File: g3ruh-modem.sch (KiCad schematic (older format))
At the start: 59 parts, among them Q1 LM7805_TO220, U1 4029, U10 LM339, U11 74HC14, U12 74HC164, U16 TL084, U2 27C128, U3 4029, U4 74HC164, U5 74HC74, U6 74HC86, U7 74HC164, U8 74HC161, U9 ZN429E-8

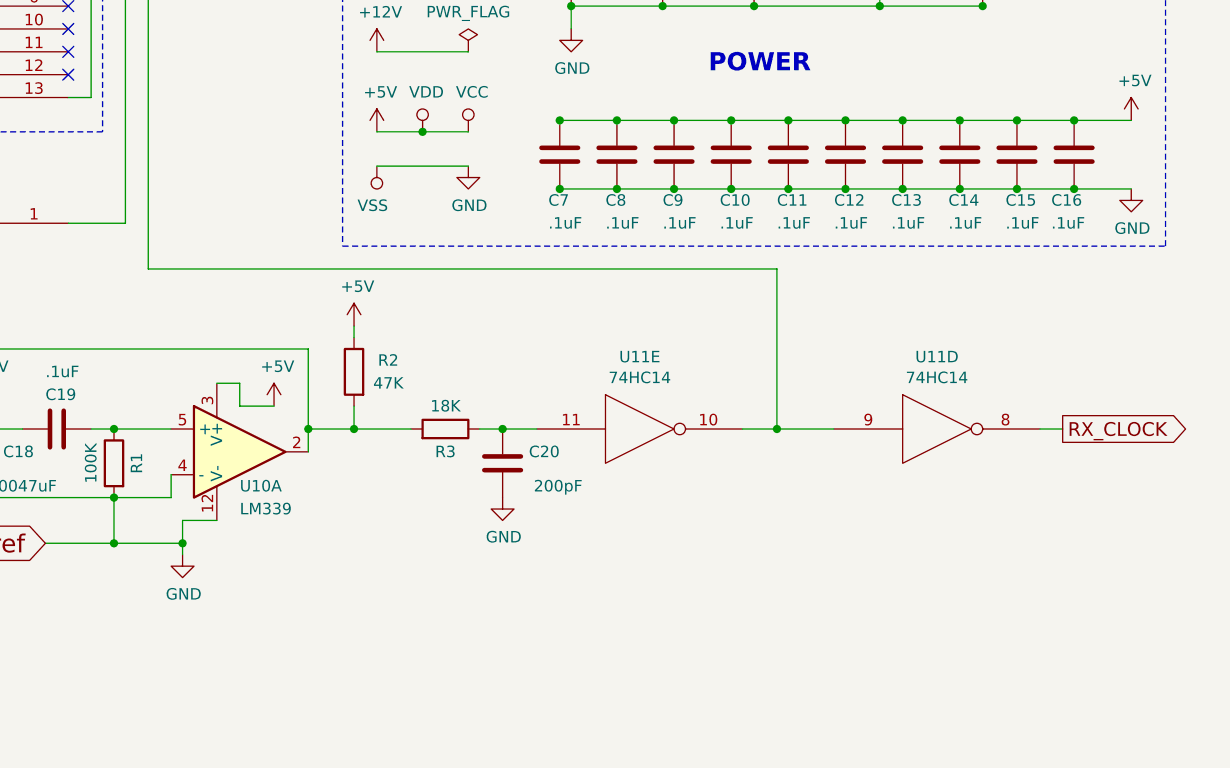
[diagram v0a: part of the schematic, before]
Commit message: Parts in roughly the right places and footprints verified.
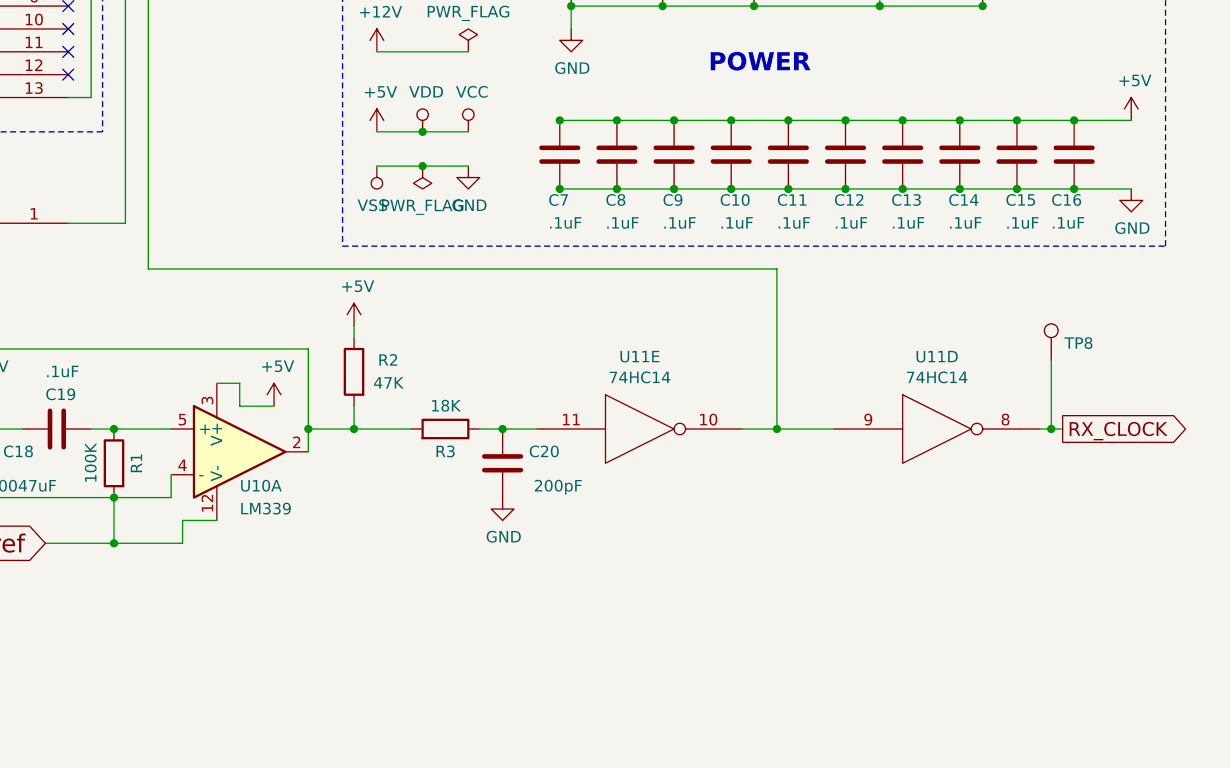
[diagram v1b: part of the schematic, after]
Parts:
- added TP8: TEST_1P, Connectors:PINTST, symbol TEST_1P
- C18, C19, C20, C21, C22: footprint Capacitors_THT:C_Axial_L3.8mm_D2.6mm_P10.00mm_Horizontal -> Capacitors_THT:C_Disc_D3.0mm_W2.0mm_P2.50mm
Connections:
- net GND: no longer C18.2, C26.2, C28.2, R1.2, R16.2, U10.12 (V-), U10.4 (-), U10.6 (-)
- net RX_CLOCK: now also TP8.1
- new net Vref: C18.2, C26.2, C28.2, R1.2, R16.2, U10.12 (V-), U10.4 (-), U10.6 (-)
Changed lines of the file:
@@
 F 0 "C22" H 8815 2646 50  0000 L CNN
 F 1 ".1uF" H 8815 2555 50  0000 L CNN
-F 2 "Capacitors_THT:C_Axial_L3.8mm_D2.6mm_P10.00mm_Horizontal" H 8738 2450 50  0001 C CNN
+F 2 "Capacitors_THT:C_Disc_D3.0mm_W2.0mm_P2.50mm" H 8738 2450 50  0001 C CNN
 F 3 "" H 8700 2600 50  0001 C CNN
 F 4 "20% monolithic" V 8700 2600 60  0001 C CNN "Type"
@@
 F 0 "C21" H 8415 2646 50  0000 L CNN
 F 1 ".1uF" H 8415 2555 50  0000 L CNN
-F 2 "Capacitors_THT:C_Axial_L3.8mm_D2.6mm_P10.00mm_Horizontal" H 8338 2450 50  0001 C CNN
+F 2 "Capacitors_THT:C_Disc_D3.0mm_W2.0mm_P2.50mm" H 8338 2450 50  0001 C CNN
 F 3 "" H 8300 2600 50  0001 C CNN
 F 4 "20% monolithic" V 8300 2600 60  0001 C CNN "Type"
@@
 F 0 "C18" H 5650 6150 50  0000 L CNN
 F 1 ".0047uF" H 5550 6000 50  0000 L CNN
-F 2 "Capacitors_THT:C_Axial_L3.8mm_D2.6mm_P10.00mm_Horizontal" H 5938 5950 50  0001 C CNN
+F 2 "Capacitors_THT:C_Disc_D3.0mm_W2.0mm_P2.50mm" H 5938 5950 50  0001 C CNN
 F 3 "" H 5900 6100 50  0001 C CNN
 F 4 "20% monolithic" V 5900 6100 60  0001 C CNN "Type"
@@
 F 0 "C19" V 6100 5900 50  0000 L CNN
 F 1 ".1uF" V 6000 5900 50  0000 L CNN
-F 2 "Capacitors_THT:C_Axial_L3.8mm_D2.6mm_P10.00mm_Horizontal" H 6288 5800 50  0001 C CNN
+F 2 "Capacitors_THT:C_Disc_D3.0mm_W2.0mm_P2.50mm" H 6288 5800 50  0001 C CNN
 F 3 "" H 6250 5950 50  0001 C CNN
 F 4 "20% monolithic" V 6250 5950 60  0001 C CNN "Type"
@@
 	1    0    0    -1
 $EndComp
-$Comp
-L GND #PWR025
-U 1 1 5972B70D
-P 6800 6500
-F 0 "#PWR025" H 6800 6250 50  0001 C CNN
-F 1 "GND" H 6805 6327 50  0000 C CNN
-F 2 "" H 6800 6500 50  0001 C CNN
-F 3 "" H 6800 6500 50  0001 C CNN
-	1    6800 6500
-	1    0    0    -1
-$EndComp
 Wire Wire Line
 	6950 6350 6800 6350
-Wire Wire Line
-	6800 6350 6800 6500
 Wire Wire Line
 	6400 5950 6750 5950
@@
 	7050 5850 7200 5850
 $Comp
-L +5V #PWR026
+L +5V #PWR025
 U 1 1 59730602
 P 7550 5500
-F 0 "#PWR026" H 7550 5350 50  0001 C CNN
+F 0 "#PWR025" H 7550 5350 50  0001 C CNN
 F 1 "+5V" H 7565 5673 50  0000 C CNN
 F 2 "" H 7550 5500 50  0001 C CNN
@@
 F 0 "C20" H 7950 6150 50  0000 L CNN
 F 1 "200pF" H 7850 6000 50  0000 L CNN
-F 2 "Capacitors_THT:C_Axial_L3.8mm_D2.6mm_P10.00mm_Horizontal" H 8238 5950 50  0001 C CNN
+F 2 "Capacitors_THT:C_Disc_D3.0mm_W2.0mm_P2.50mm" H 8238 5950 50  0001 C CNN
 F 3 "" H 8200 6100 50  0001 C CNN
 F 4 "20% monolithic" V 8200 6100 60  0001 C CNN "Type"
@@
 $EndComp
 $Comp
-L GND #PWR027
+L GND #PWR026
 U 1 1 597318B4
 P 8200 6250
-F 0 "#PWR027" H 8200 6000 50  0001 C CNN
+F 0 "#PWR026" H 8200 6000 50  0001 C CNN
 F 1 "GND" H 8205 6077 50  0000 C CNN
 F 2 "" H 8200 6250 50  0001 C CNN
@@
 	7950 3700 8100 3700
 $Comp
-L +5V #PWR028
+L +5V #PWR027
 U 1 1 596EEE17
 P 10300 3550
-F 0 "#PWR028" H 10300 3400 50  0001 C CNN
+F 0 "#PWR027" H 10300 3400 50  0001 C CNN
 F 1 "+5V" H 10315 3723 50  0000 C CNN
 F 2 "" H 10300 3550 50  0001 C CNN
@@
 	8450 4900 10950 4900
 $Comp
-L +5V #PWR029
+L +5V #PWR028
 U 1 1 596F0936
 P 10950 4600
-F 0 "#PWR029" H 10950 4450 50  0001 C CNN
+F 0 "#PWR028" H 10950 4450 50  0001 C CNN
 F 1 "+5V" H 10965 4773 50  0000 C CNN
 F 2 "" H 10950 4600 50  0001 C CNN
@@
 $EndComp
 $Comp
-L GND #PWR030
+L GND #PWR029
 U 1 1 596F10F5
 P 10950 4900
-F 0 "#PWR030" H 10950 4650 50  0001 C CNN
+F 0 "#PWR029" H 10950 4650 50  0001 C CNN
 F 1 "GND" H 10955 4727 50  0000 C CNN
 F 2 "" H 10950 4900 50  0001 C CNN
@@
 Connection ~ 8500 4100
 $Comp
-L GND #PWR031
+L GND #PWR030
 U 1 1 596F18F3
 P 8050 4800
-F 0 "#PWR031" H 8050 4550 50  0001 C CNN
+F 0 "#PWR030" H 8050 4550 50  0001 C CNN
 F 1 "GND" H 8055 4627 50  0000 C CNN
 F 2 "" H 8050 4800 50  0001 C CNN
@@
 Connection ~ 4050 3850
 $Comp
-L GND #PWR032
+L GND #PWR031
 U 1 1 597348D5
 P 1300 3700
-F 0 "#PWR032" H 1300 3450 50  0001 C CNN
+F 0 "#PWR031" H 1300 3450 50  0001 C CNN
 F 1 "GND" H 1305 3527 50  0000 C CNN
 F 2 "" H 1300 3700 50  0001 C CNN
@@
 $EndComp
 $Comp
-L GND #PWR033
+L GND #PWR032
 U 1 1 59734EC4
 P 1700 2950
-F 0 "#PWR033" H 1700 2700 50  0001 C CNN
+F 0 "#PWR032" H 1700 2700 50  0001 C CNN
 F 1 "GND" H 1705 2777 50  0000 C CNN
 F 2 "" H 1700 2950 50  0001 C CNN
@@
 $EndComp
 $Comp
-L GND #PWR034
+L GND #PWR033
 U 1 1 597366E0
 P 1300 4950
-F 0 "#PWR034" H 1300 4700 50  0001 C CNN
+F 0 "#PWR033" H 1300 4700 50  0001 C CNN
 F 1 "GND" H 1305 4777 50  0000 C CNN
 F 2 "" H 1300 4950 50  0001 C CNN
@@
 	1300 4850 1300 4950
 $Comp
-L GND #PWR035
+L GND #PWR034
 U 1 1 59737386
 P 3250 5050
-F 0 "#PWR035" H 3250 4800 50  0001 C CNN
+F 0 "#PWR034" H 3250 4800 50  0001 C CNN
 F 1 "GND" H 3255 4877 50  0000 C CNN
 F 2 "" H 3250 5050 50  0001 C CNN
@@
 Wire Wire Line
 	5900 6250 6750 6250
-Connection ~ 6800 6450
 Connection ~ 6500 6450
 $Comp
-L GND #PWR036
+L GND #PWR035
 U 1 1 5976EA92
 P 650 6900
-F 0 "#PWR036" H 650 6650 50  0001 C CNN
+F 0 "#PWR035" H 650 6650 50  0001 C CNN
 F 1 "GND" H 655 6727 50  0000 C CNN
 F 2 "" H 650 6900 50  0001 C CNN
@@
 Connection ~ 650  6750
 $Comp
-L GND #PWR037
+L GND #PWR036
 U 1 1 59773189
 P 3050 3500
-F 0 "#PWR037" H 3050 3250 50  0001 C CNN
+F 0 "#PWR036" H 3050 3250 50  0001 C CNN
 F 1 "GND" H 3055 3327 50  0000 C CNN
 F 2 "" H 3050 3500 50  0001 C CNN
@@
 	8450 4600 10950 4600
 $Comp
-L +12V #PWR038
+L +12V #PWR037
 U 1 1 596F8E90
 P 8500 3600
-F 0 "#PWR038" H 8500 3450 50  0001 C CNN
+F 0 "#PWR037" H 8500 3450 50  0001 C CNN
 F 1 "+12V" H 8515 3773 50  0000 C CNN
 F 2 "" H 8500 3600 50  0001 C CNN
@@
 $EndComp
 $Comp
-L PWR_FLAG #FLG039
+L PWR_FLAG #FLG038
 U 1 1 596FCD3F
 P 8050 4300
-F 0 "#FLG039" H 8050 4375 50  0001 C CNN
+F 0 "#FLG038" H 8050 4375 50  0001 C CNN
 F 1 "PWR_FLAG" H 8050 4474 50  0000 C CNN
 F 2 "" H 8050 4300 50  0001 C CNN
@@
 $EndComp
 $Comp
-L +12V #PWR040
+L +12V #PWR039
 U 1 1 596FFF3D
 P 2900 2750
-F 0 "#PWR040" H 2900 2600 50  0001 C CNN
+F 0 "#PWR039" H 2900 2600 50  0001 C CNN
 F 1 "+12V" H 2915 2923 50  0000 C CNN
 F 2 "" H 2900 2750 50  0001 C CNN
@@
 	2900 2900 2900 2750
 $Comp
-L VSS #PWR041
+L VSS #PWR040
 U 1 1 597029AB
 P 7650 4800
-F 0 "#PWR041" H 7650 4650 50  0001 C CNN
+F 0 "#PWR040" H 7650 4650 50  0001 C CNN
 F 1 "VSS" H 7668 4973 50  0000 C CNN
 F 2 "" H 7650 4800 50  0001 C CNN
@@
 	8900 3700 8900 3800
 $Comp
-L +5V #PWR042
+L +5V #PWR041
 U 1 1 5970428A
 P 7650 4650
-F 0 "#PWR042" H 7650 4500 50  0001 C CNN
+F 0 "#PWR041" H 7650 4500 50  0001 C CNN
 F 1 "+5V" H 7665 4823 50  0000 C CNN
 F 2 "" H 7650 4650 50  0001 C CNN
@@
 $EndComp
 $Comp
-L VCC #PWR043
+L VCC #PWR042
 U 1 1 5970436D
 P 8050 4650
-F 0 "#PWR043" H 8050 4500 50  0001 C CNN
+F 0 "#PWR042" H 8050 4500 50  0001 C CNN
 F 1 "VCC" H 8067 4823 50  0000 C CNN
 F 2 "" H 8050 4650 50  0001 C CNN
@@
 	8500 4100 10300 4100
 $Comp
-L GND #PWR044
+L GND #PWR043
 U 1 1 59704F68
 P 8500 4200
-F 0 "#PWR044" H 8500 3950 50  0001 C CNN
+F 0 "#PWR043" H 8500 3950 50  0001 C CNN
 F 1 "GND" H 8505 4027 50  0000 C CNN
 F 2 "" H 8500 4200 50  0001 C CNN
@@
 	8500 4200 8500 4100
 $Comp
-L +12V #PWR045
+L +12V #PWR044
 U 1 1 596F1C01
 P 7650 4300
-F 0 "#PWR045" H 7650 4150 50  0001 C CNN
+F 0 "#PWR044" H 7650 4150 50  0001 C CNN
 F 1 "+12V" H 7665 4473 50  0000 C CNN
 F 2 "" H 7650 4300 50  0001 C CNN
@@
 $EndComp
 $Comp
-L VDD #PWR046
+L VDD #PWR045
 U 1 1 596F2F8C
 P 7850 4650
-F 0 "#PWR046" H 7850 4500 50  0001 C CNN
+F 0 "#PWR045" H 7850 4500 50  0001 C CNN
 F 1 "VDD" H 7867 4823 50  0000 C CNN
 F 2 "" H 7850 4650 50  0001 C CNN
@@
 $EndComp
 Connection ~ 7850 4650
+$Comp
+L TEST_1P TP8
+U 1 1 597016E3
+P 10600 5650
+F 0 "TP8" H 10658 5724 50  0000 L CNN
+F 1 "TEST_1P" H 10658 5679 50  0001 L CNN
+F 2 "Connectors:PINTST" H 10800 5650 50  0001 C CNN
+F 3 "" H 10800 5650 50  0001 C CNN
+	1    10600 5650
+	1    0    0    -1
+$EndComp
+Wire Wire Line
+	10600 5650 10600 5950
+Connection ~ 10600 5950
+Wire Wire Line
+	6800 6450 6800 6350
+$Comp
+L PWR_FLAG #FLG046
+U 1 1 59706E06
+P 7850 4800
+F 0 "#FLG046" H 7850 4875 50  0001 C CNN
+F 1 "PWR_FLAG" H 7850 4974 50  0000 C CNN
+F 2 "" H 7850 4800 50  0001 C CNN
+F 3 "" H 7850 4800 50  0001 C CNN
+	1    7850 4800
+	1    0    0    1
+$EndComp
+Connection ~ 7850 4800
 $EndSCHEMATC

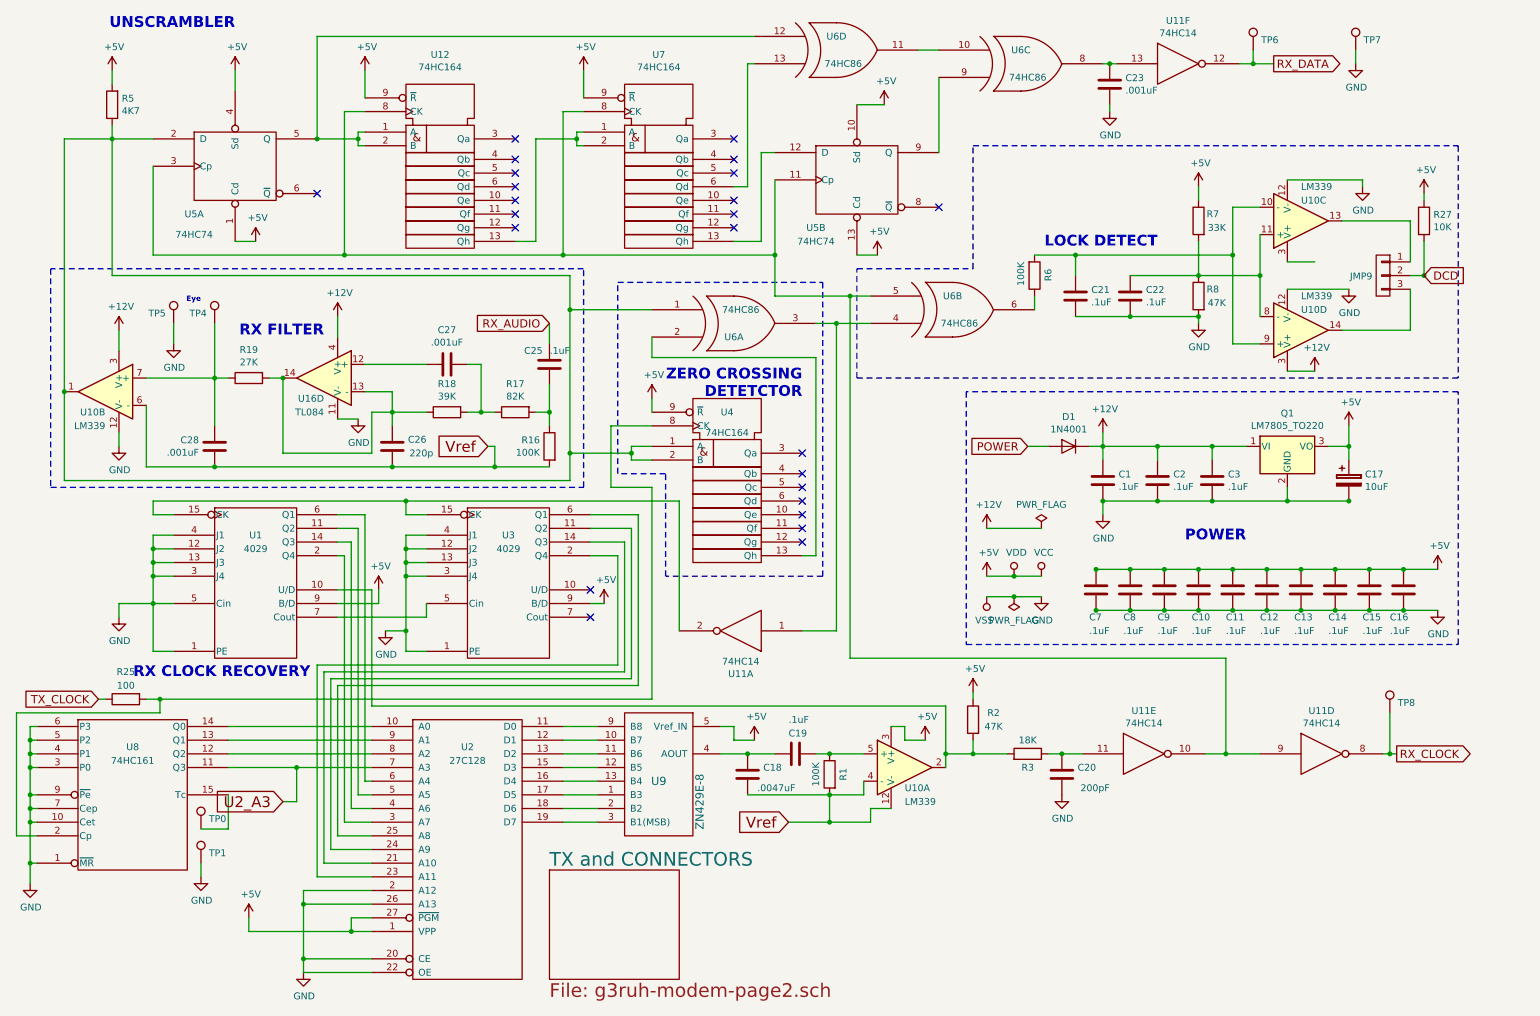
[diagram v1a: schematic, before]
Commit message: Switched over to Kicad's hierachical sheets.  There are problems.
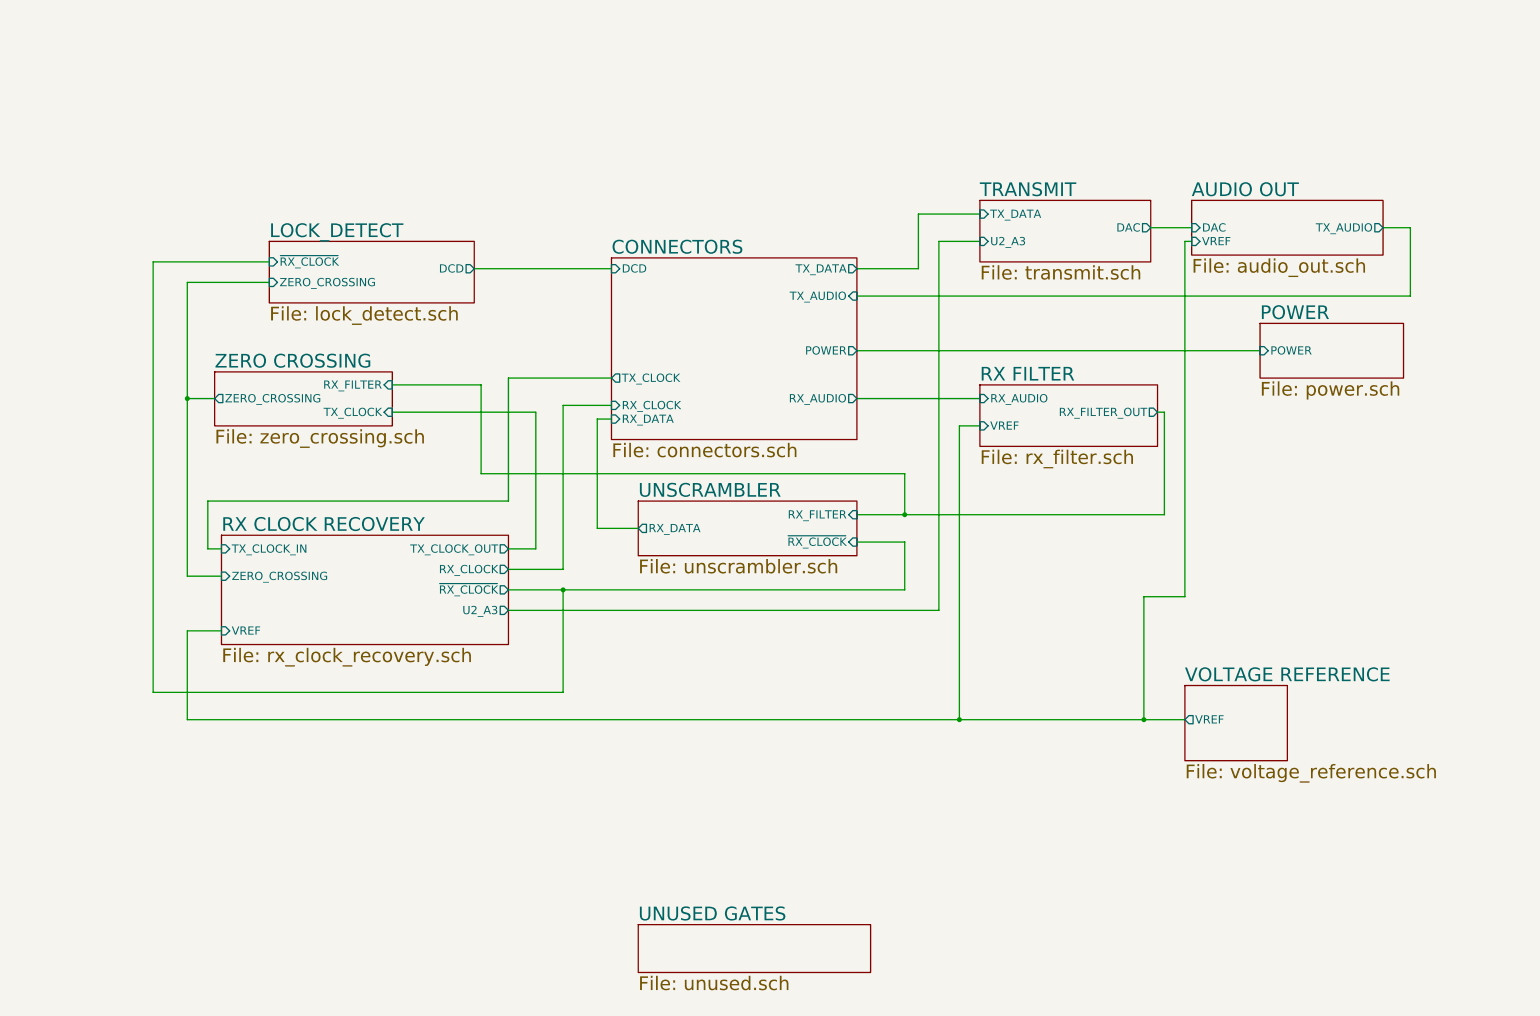
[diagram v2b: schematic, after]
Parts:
- removed C1, C10, C11, C12, C13, C14, C15, C16, C19, C2, C21, C22, C25, C3, C7, C8, C9: .1uF, Capacitors_THT:C_Disc_D3.0mm_W2.0mm_P2.50mm, symbol C
- removed C17: 10uF, Capacitors_THT:CP_Radial_Tantal_D5.0mm_P5.00mm, symbol CP
- removed C18: .0047uF, Capacitors_THT:C_Disc_D3.0mm_W2.0mm_P2.50mm, symbol C
- removed C20: 200pF, Capacitors_THT:C_Disc_D3.0mm_W2.0mm_P2.50mm, symbol C
- removed C23, C27, C28: .001uF, Capacitors_THT:C_Axial_L3.8mm_D2.6mm_P10.00mm_Horizontal, symbol C
- removed C26: 220p, Capacitors_THT:C_Axial_L3.8mm_D2.6mm_P10.00mm_Horizontal, symbol C
- removed D1: 1N4001, Diodes_THT:D_DO-41_SOD81_P7.62mm_Horizontal, symbol D
- removed JMP9: CONN_01X03, Pin_Headers:Pin_Header_Straight_1x03_Pitch2.54mm, symbol CONN_01X03
- removed Q1: LM7805_TO220, TO_SOT_Packages_THT:TO-220_Horizontal, symbol LM7805_TO220
- removed R1, R16, R6: 100K, Resistors_THT:R_Axial_DIN0204_L3.6mm_D1.6mm_P7.62mm_Horizontal, symbol R
- removed R17: 82K, Resistors_THT:R_Axial_DIN0204_L3.6mm_D1.6mm_P7.62mm_Horizontal, symbol R
- removed R18: 39K, Resistors_THT:R_Axial_DIN0204_L3.6mm_D1.6mm_P7.62mm_Horizontal, symbol R
- removed R19: 27K, Resistors_THT:R_Axial_DIN0204_L3.6mm_D1.6mm_P7.62mm_Horizontal, symbol R
- removed R2, R8: 47K, Resistors_THT:R_Axial_DIN0204_L3.6mm_D1.6mm_P7.62mm_Horizontal, symbol R
- removed R25: 100, Resistors_THT:R_Axial_DIN0204_L3.6mm_D1.6mm_P7.62mm_Horizontal, symbol R
- removed R27: 10K, Resistors_THT:R_Axial_DIN0204_L3.6mm_D1.6mm_P7.62mm_Horizontal, symbol R
- removed R3: 18K, Resistors_THT:R_Axial_DIN0204_L3.6mm_D1.6mm_P7.62mm_Horizontal, symbol R
- removed R5: 4K7, Resistors_THT:R_Axial_DIN0204_L3.6mm_D1.6mm_P7.62mm_Horizontal, symbol R
- removed R7: 33K, Resistors_THT:R_Axial_DIN0204_L3.6mm_D1.6mm_P7.62mm_Horizontal, symbol R
- removed TP0, TP1, TP4, TP5, TP6, TP7, TP8: TEST_1P, Connectors:PINTST, symbol TEST_1P
- removed U1, U3: 4029, Housings_DIP:DIP-16_W7.62mm_Socket, symbol 4029
- removed U10: LM339, Housings_DIP:DIP-14_W7.62mm, symbol LM339
- removed U11: 74HC14, Housings_DIP:DIP-14_W7.62mm, symbol 74HC14
- removed U12, U4, U7: 74HC164, Housings_DIP:DIP-14_W7.62mm, symbol 74164
- removed U16: TL084, Housings_DIP:DIP-14_W7.62mm_Socket, symbol TL084
- removed U2: 27C128, Housings_DIP:DIP-28_W15.24mm, symbol 27C128
- removed U5: 74HC74, Housings_DIP:DIP-14_W7.62mm, symbol 74HC74
- removed U6: 74HC86, Housings_DIP:DIP-14_W7.62mm, symbol 74HC86
- removed U8: 74HC161, Housings_DIP:DIP-16_W7.62mm, symbol 74LS161
- removed U9: ZN429E-8, Housings_DIP:DIP-14_W7.62mm_Socket, symbol ZN429E-8
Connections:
- net labels removed: +12V, +5V, DCD, GND, POWER, RX_AUDIO, RX_CLOCK, RX_DATA, TX_CLOCK, U2_A3, VCC, VDD, VSS, Vref
- wire segments 257 -> 54
- no-connect marks 24 -> 0
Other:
- note removed: "Eye"
- note removed: "LOCK DETECT"
- note removed: "POWER\n"
- note removed: "RX CLOCK RECOVERY"
- note removed: "RX FILTER"
- note removed: "UNSCRAMBLER\n"
- note removed: "ZERO CROSSING\nDETETCTOR"
